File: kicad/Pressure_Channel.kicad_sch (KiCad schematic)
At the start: 1 part

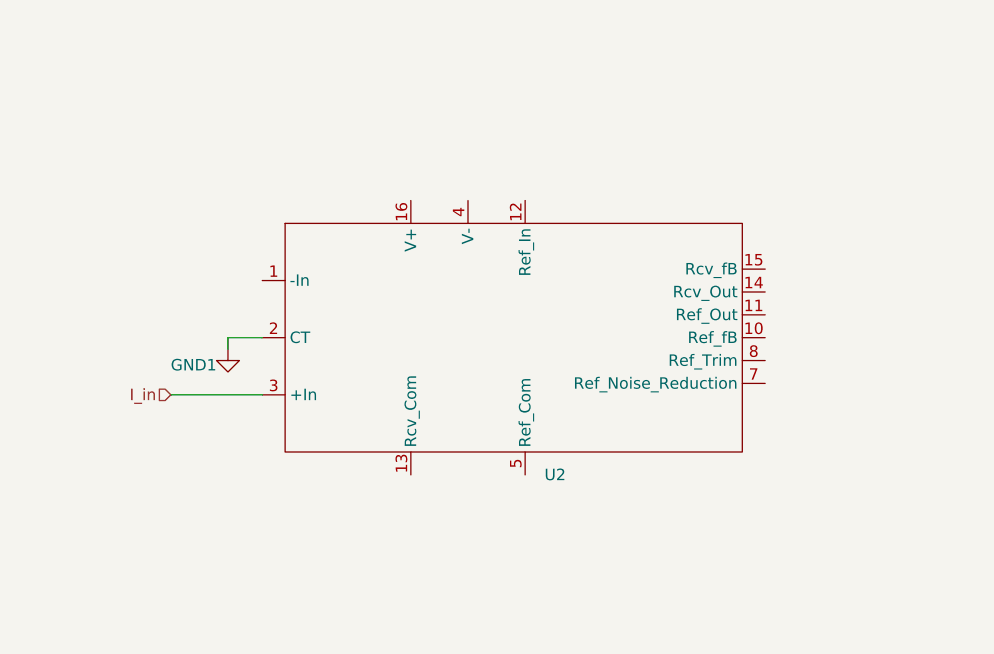
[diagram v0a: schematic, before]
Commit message: finished RCV420 channel sheet with capacitors for smoothing, reistor for protection, options TVS, and labels, now working on top sheet connections
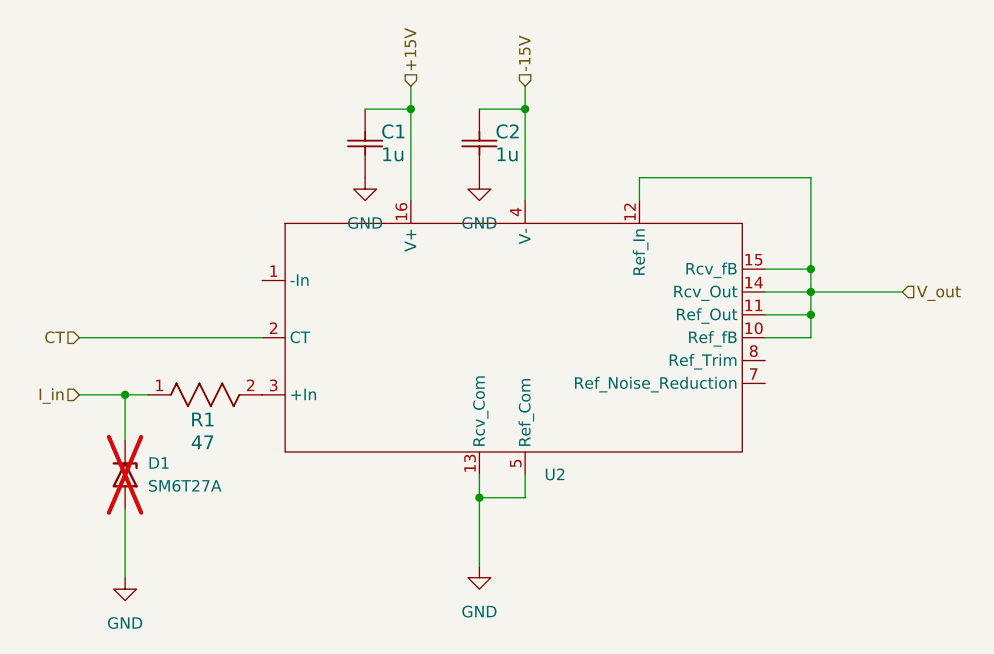
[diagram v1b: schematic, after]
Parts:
- added C1, C2: 1u, CAP_PAN_6.3X11.2_PAN, symbol Pressure:ECA2EM010B
- added D1: SM6T27A, Diode_SMD:D_SMB, symbol Diode:SM6T27A
- added R1: 47, RES_CHP2512_BRN, symbol Pressure:CHP2512AFX-47R0ELF
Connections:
- net I_in: now also D1.1 (A1), R1.1; no longer U2.3 (+In)
- net V_out: now reaches U2.10 (Ref_fB)
- net V_out: now also U2.11 (Ref_Out), U2.12 (Ref_In), U2.14 (Rcv_Out), U2.15 (Rcv_fB)
- net GND: now reaches U2.13 (Rcv_Com)
- net GND: now also U2.5 (Ref_Com), C1.1, C2.1, D1.2 (A2)
- net +15V: now reaches U2.16 (V+)
- net +15V: now also C1.2
- net -15V: now reaches U2.4 (V-)
- net -15V: now also C2.2
- net GND1 renamed CT
- new net: R1.2, U2.3 (+In)
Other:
- company: (none) -> JRPD
- title: (none) -> Single Pressure Channel

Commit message: began pcb layout
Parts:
- removed C1, C2: 1u, CAP_PAN_6.3X11.2_PAN, symbol Pressure:ECA2EM010B
- added C1, C4: 1u, Capacitor_SMD:C_0805_2012Metric_Pad1.18x1.45mm_HandSolder, symbol Device:C
- D1: value SM6T27A -> TVS
- R1: footprint RES_CHP2512_BRN -> Resistor_SMD:R_2512_6332Metric_Pad1.40x3.35mm_HandSolder
- U2: footprint (none) -> Package_DIP:DIP-16_W7.62mm
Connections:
- net +15V: now also C1.1
- net -15V: now also C4.1
- net GND: now also C1.2, C4.2
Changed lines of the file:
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@@
+	)
+	(symbol
+		(lib_id "Device:C")
+		(at 135.89 67.31 0)
+		(unit 1)
+		(body_style 1)
+		(exclude_from_sim no)
+		(in_bom yes)
+		(on_board yes)
+		(in_pos_files yes)
+		(dnp no)
+		(property "Reference" "C1"
+			(at 130.556 65.532 0)
+			(show_name no)
+			(do_not_autoplace no)
+			(effects
+				(font
+					(size 1.27 1.27)
+				)
+				(justify left)
+			)
+		)
+		(property "Value" "1u"
+			(at 130.81 67.818 0)
+			(show_name no)
+			(do_not_autoplace no)
+			(effects
+				(font
+					(size 1.27 1.27)
+				)
+				(justify left)
+			)
+		)
+		(property "Footprint" "Capacitor_SMD:C_0805_2012Metric_Pad1.18x1.45mm_HandSolder"
+			(at 136.8552 71.12 0)
+			(hide yes)
+			(show_name no)
+			(do_not_autoplace no)
+			(effects
+				(font
+					(size 1.27 1.27)
+				)
+			)
+		)
+		(property "Datasheet" ""
+			(at 135.89 67.31 0)
+			(hide yes)
+			(show_name no)
+			(do_not_autoplace no)
+			(effects
+				(font
+					(size 1.27 1.27)
+				)
+			)
+		)
+		(property "Description" "Unpolarized capacitor"
+			(at 135.89 67.31 0)
+			(hide yes)
+			(show_name no)
+			(do_not_autoplace no)
+			(effects
+				(font
+					(size 1.27 1.27)
+				)
+			)
+		)
+		(pin "2"
+		)
+		(pin "1"
+		)
+		(instances
+			(project "pressure_conditioner"
+				(path "/d1a2bab1-03ca-4de0-a936-00ed771cb4f3/37aadd6b-2f24-4a7a-95b6-36c8865998ad"
+					(reference "C1")
+					(unit 1)
+				)
+				(path "/d1a2bab1-03ca-4de0-a936-00ed771cb4f3/d1451d03-fec6-4cbb-9f6d-c808002a48c4"
+					(reference "C2")
+					(unit 1)
+				)
+				(path "/d1a2bab1-03ca-4de0-a936-00ed771cb4f3/db7fca88-321a-44d3-ab15-233d0aa15f41"
+					(reference "C3")
+					(unit 1)
+				)
+			)
+		)
 	)
 	(symbol
@@
 			)
 		)
-		(property "Footprint" "RES_CHP2512_BRN"
+		(property "Footprint" "Resistor_SMD:R_2512_6332Metric_Pad1.40x3.35mm_HandSolder"
 			(at 111.76 95.25 0)
 			(hide yes)
@@
 			)
 		)
-		(property "Value" "SM6T27A"
+		(property "Value" "TVS"
 			(at 111.76 105.4099 90)
 			(show_name no)
@@
 	)
 	(symbol
-		(lib_id "Pressure:ECA2EM010B")
-		(at 135.89 71.12 90)
-		(unit 1)
-		(body_style 1)
-		(exclude_from_sim no)
-		(in_bom yes)
-		(on_board yes)
-		(in_pos_files yes)
-		(dnp no)
-		(property "Reference" "C1"
-			(at 137.668 66.04 90)
-			(show_name no)
-			(do_not_autoplace no)
-			(effects
-				(font
-					(size 1.524 1.524)
-				)
-				(justify right)
-			)
-		)
-		(property "Value" "1u"
-			(at 137.668 68.58 90)
-			(show_name no)
-			(do_not_autoplace no)
-			(effects
-				(font
-					(size 1.524 1.524)
-				)
-				(justify right)
-			)
-		)
-		(property "Footprint" "CAP_PAN_6.3X11.2_PAN"
-			(at 135.89 71.12 0)
-			(hide yes)
-			(show_name no)
-			(do_not_autoplace no)
-			(effects
-				(font
-					(size 1.27 1.27)
-					(italic yes)
-				)
-			)
-		)
-		(property "Datasheet" "ECA2EM010B"
-			(at 135.89 71.12 0)
-			(hide yes)
-			(show_name no)
-			(do_not_autoplace no)
-			(effects
-				(font
-					(size 1.27 1.27)
-					(italic yes)
-				)
-			)
-		)
-		(property "Description" ""
-			(at 135.89 71.12 0)
-			(hide yes)
-			(show_name no)
-			(do_not_autoplace no)
-			(effects
-				(font
-					(size 1.27 1.27)
-				)
-			)
-		)
-		(pin "2"
-		)
-		(pin "1"
-		)
-		(instances
-			(project "pressure_conditioner"
-				(path "/d1a2bab1-03ca-4de0-a936-00ed771cb4f3/37aadd6b-2f24-4a7a-95b6-36c8865998ad"
-					(reference "C1")
-					(unit 1)
-				)
-				(path "/d1a2bab1-03ca-4de0-a936-00ed771cb4f3/d1451d03-fec6-4cbb-9f6d-c808002a48c4"
-					(reference "C3")
-					(unit 1)
-				)
-				(path "/d1a2bab1-03ca-4de0-a936-00ed771cb4f3/db7fca88-321a-44d3-ab15-233d0aa15f41"
-					(reference "C5")
-					(unit 1)
-				)
-			)
-		)
-	)
-	(symbol
 		(lib_id "power:GND")
 		(at 135.89 71.12 0)
@@
 	)
 	(symbol
-		(lib_id "Pressure:ECA2EM010B")
-		(at 148.59 71.12 90)
+		(lib_id "Device:C")
+		(at 148.59 67.31 0)
 		(unit 1)
 		(body_style 1)
@@
 		(in_pos_files yes)
 		(dnp no)
-		(property "Reference" "C2"
-			(at 150.368 66.04 90)
-			(show_name no)
-			(do_not_autoplace no)
-			(effects
-				(font
-					(size 1.524 1.524)
-				)
-				(justify right)
+		(property "Reference" "C4"
+			(at 143.256 65.786 0)
+			(show_name no)
+			(do_not_autoplace no)
+			(effects
+				(font
+					(size 1.27 1.27)
+				)
+				(justify left)
 			)
 		)
 		(property "Value" "1u"
-			(at 150.368 68.58 90)
-			(show_name no)
-			(do_not_autoplace no)
-			(effects
-				(font
-					(size 1.524 1.524)
-				)
-				(justify right)
-			)
-		)
-		(property "Footprint" "CAP_PAN_6.3X11.2_PAN"
-			(at 148.59 71.12 0)
-			(hide yes)
-			(show_name no)
-			(do_not_autoplace no)
-			(effects
-				(font
-					(size 1.27 1.27)
-					(italic yes)
-				)
-			)
-		)
-		(property "Datasheet" "ECA2EM010B"
-			(at 148.59 71.12 0)
-			(hide yes)
-			(show_name no)
-			(do_not_autoplace no)
-			(effects
-				(font
-					(size 1.27 1.27)
-					(italic yes)
-				)
-			)
-		)
-		(property "Description" ""
-			(at 148.59 71.12 0)
-			(hide yes)
-			(show_name no)
-			(do_not_autoplace no)
-			(effects
-				(font
-					(size 1.27 1.27)
-				)
-			)
+			(at 143.51 67.818 0)
+			(show_name no)
+			(do_not_autoplace no)
+			(effects
+				(font
+					(size 1.27 1.27)
+				)
+				(justify left)
+			)
+		)
+		(property "Footprint" "Capacitor_SMD:C_0805_2012Metric_Pad1.18x1.45mm_HandSolder"
+			(at 149.5552 71.12 0)
+			(hide yes)
+			(show_name no)
+			(do_not_autoplace no)
+			(effects
+				(font
+					(size 1.27 1.27)
+				)
+			)
+		)
+		(property "Datasheet" ""
+			(at 148.59 67.31 0)
+			(hide yes)
+			(show_name no)
+			(do_not_autoplace no)
+			(effects
+				(font
+					(size 1.27 1.27)
+				)
+			)
+		)
+		(property "Description" "Unpolarized capacitor"
+			(at 148.59 67.31 0)
+			(hide yes)
+			(show_name no)
+			(do_not_autoplace no)
+			(effects
+				(font
+					(size 1.27 1.27)
+				)
+			)
+		)
+		(pin "1"
 		)
 		(pin "2"
-		)
-		(pin "1"
 		)
 		(instances
 			(project "pressure_conditioner"
 				(path "/d1a2bab1-03ca-4de0-a936-00ed771cb4f3/37aadd6b-2f24-4a7a-95b6-36c8865998ad"
-					(reference "C2")
+					(reference "C4")
 					(unit 1)
 				)
 				(path "/d1a2bab1-03ca-4de0-a936-00ed771cb4f3/d1451d03-fec6-4cbb-9f6d-c808002a48c4"
-					(reference "C4")
+					(reference "C5")
 					(unit 1)
 				)
@@
 			)
 		)
-		(property "Footprint" ""
+		(property "Footprint" "Package_DIP:DIP-16_W7.62mm"
 			(at 114.3 101.6 0)
 			(hide yes)

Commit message: Finished preliminary layout of Rev. A of board
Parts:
- U2: footprint Package_DIP:DIP-16_W7.62mm -> Package_DIP:CERDIP-16_W7.62mm_SideBrazed
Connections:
- no-connect marks 0 -> 3
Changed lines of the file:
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@@
 		(color 0 0 0 0)
+	)
+	(no_connect
+		(at 180.34 93.98)
+	)
+	(no_connect
+		(at 180.34 91.44)
+	)
+	(no_connect
+		(at 124.46 82.55)
 	)
 	(wire
@@
 	)
 	(symbol
+		(lib_id "Pressure:RCV420")
+		(at 114.3 101.6 0)
+		(unit 1)
+		(body_style 1)
+		(exclude_from_sim no)
+		(in_bom yes)
+		(on_board yes)
+		(in_pos_files yes)
+		(dnp no)
+		(fields_autoplaced yes)
+		(property "Reference" "U2"
+			(at 155.8133 104.14 0)
+			(show_name no)
+			(do_not_autoplace no)
+			(effects
+				(font
+					(size 1.27 1.27)
+				)
+				(justify left)
+			)
+		)
+		(property "Value" ""
+			(at 114.3 101.6 0)
+			(show_name no)
+			(do_not_autoplace no)
+			(effects
+				(font
+					(size 1.27 1.27)
+				)
+			)
+		)
+		(property "Footprint" "Package_DIP:CERDIP-16_W7.62mm_SideBrazed"
+			(at 114.3 101.6 0)
+			(hide yes)
+			(show_name no)
+			(do_not_autoplace no)
+			(effects
+				(font
+					(size 1.27 1.27)
+				)
+			)
+		)
+		(property "Datasheet" ""
+			(at 114.3 101.6 0)
+			(hide yes)
+			(show_name no)
+			(do_not_autoplace no)
+			(effects
+				(font
+					(size 1.27 1.27)
+				)
+			)
+		)
+		(property "Description" ""
+			(at 114.3 101.6 0)
+			(hide yes)
+			(show_name no)
+			(do_not_autoplace no)
+			(effects
+				(font
+					(size 1.27 1.27)
+				)
+			)
+		)
+		(pin "7"
+		)
+		(pin "10"
+		)
+		(pin "8"
+		)
+		(pin "11"
+		)
+		(pin "2"
+		)
+		(pin "5"
+		)
+		(pin "1"
+		)
+		(pin "3"
+		)
+		(pin "4"
+		)
+		(pin "13"
+		)
+		(pin "16"
+		)
+		(pin "14"
+		)
+		(pin "12"
+		)
+		(pin "15"
+		)
+		(instances
+			(project "pressure_conditioner"
+				(path "/d1a2bab1-03ca-4de0-a936-00ed771cb4f3/37aadd6b-2f24-4a7a-95b6-36c8865998ad"
+					(reference "U2")
+					(unit 1)
+				)
+				(path "/d1a2bab1-03ca-4de0-a936-00ed771cb4f3/d1451d03-fec6-4cbb-9f6d-c808002a48c4"
+					(reference "U3")
+					(unit 1)
+				)
+				(path "/d1a2bab1-03ca-4de0-a936-00ed771cb4f3/db7fca88-321a-44d3-ab15-233d0aa15f41"
+					(reference "U4")
+					(unit 1)
+				)
+			)
+		)
+	)
+	(symbol
 		(lib_id "Device:C")
 		(at 135.89 67.31 0)
@@
 					(unit 1)
 				)
-			)
-		)
-	)
-	(symbol
-		(lib_id "Pressure:RCV420")
-		(at 114.3 101.6 0)
-		(unit 1)
-		(body_style 1)
-		(exclude_from_sim no)
-		(in_bom yes)
-		(on_board yes)
-		(in_pos_files yes)
-		(dnp no)
-		(fields_autoplaced yes)
-		(property "Reference" "U2"
-			(at 155.8133 104.14 0)
-			(show_name no)
-			(do_not_autoplace no)
-			(effects
-				(font
-					(size 1.27 1.27)
-				)
-				(justify left)
-			)
-		)
-		(property "Value" ""
-			(at 114.3 101.6 0)
-			(show_name no)
-			(do_not_autoplace no)
-			(effects
-				(font
-					(size 1.27 1.27)
-				)
-			)
-		)
-		(property "Footprint" "Package_DIP:DIP-16_W7.62mm"
-			(at 114.3 101.6 0)
-			(hide yes)
-			(show_name no)
-			(do_not_autoplace no)
-			(effects
-				(font
-					(size 1.27 1.27)
-				)
-			)
-		)
-		(property "Datasheet" ""
-			(at 114.3 101.6 0)
-			(hide yes)
-			(show_name no)
-			(do_not_autoplace no)
-			(effects
-				(font
-					(size 1.27 1.27)
-				)
-			)
-		)
-		(property "Description" ""
-			(at 114.3 101.6 0)
-			(hide yes)
-			(show_name no)
-			(do_not_autoplace no)
-			(effects
-				(font
-					(size 1.27 1.27)
-				)
-			)
-		)
-		(pin "2"
-		)
-		(pin "13"
-		)
-		(pin "10"
-		)
-		(pin "4"
-		)
-		(pin "1"
-		)
-		(pin "5"
-		)
-		(pin "3"
-		)
-		(pin "7"
-		)
-		(pin "8"
-		)
-		(pin "11"
-		)
-		(pin "12"
-		)
-		(pin "16"
-		)
-		(pin "14"
-		)
-		(pin "15"
-		)
-		(instances
-			(project "pressure_conditioner"
-				(path "/d1a2bab1-03ca-4de0-a936-00ed771cb4f3/37aadd6b-2f24-4a7a-95b6-36c8865998ad"
-					(reference "U2")
-					(unit 1)
-				)
-				(path "/d1a2bab1-03ca-4de0-a936-00ed771cb4f3/d1451d03-fec6-4cbb-9f6d-c808002a48c4"
-					(reference "U3")
-					(unit 1)
-				)
-				(path "/d1a2bab1-03ca-4de0-a936-00ed771cb4f3/db7fca88-321a-44d3-ab15-233d0aa15f41"
-					(reference "U4")
-					(unit 1)
-				)
